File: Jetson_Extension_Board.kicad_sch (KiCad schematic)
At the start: 2 parts, among them J6 40_Pin_Jetson_Connector, SW1 SW_Push_DPDT

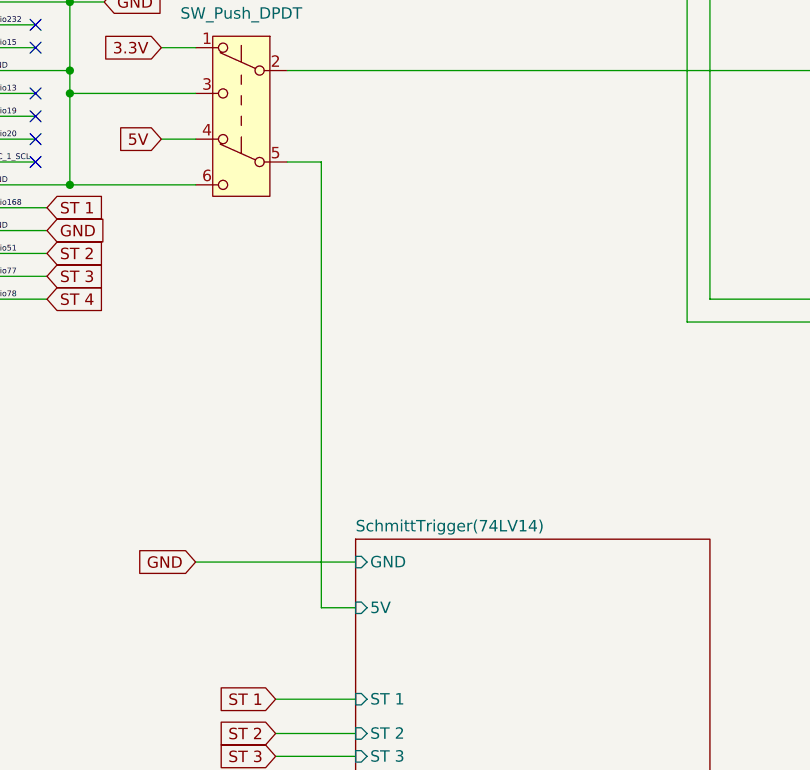
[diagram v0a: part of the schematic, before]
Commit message: Pluh 1 and 2 removed, main file is updated version
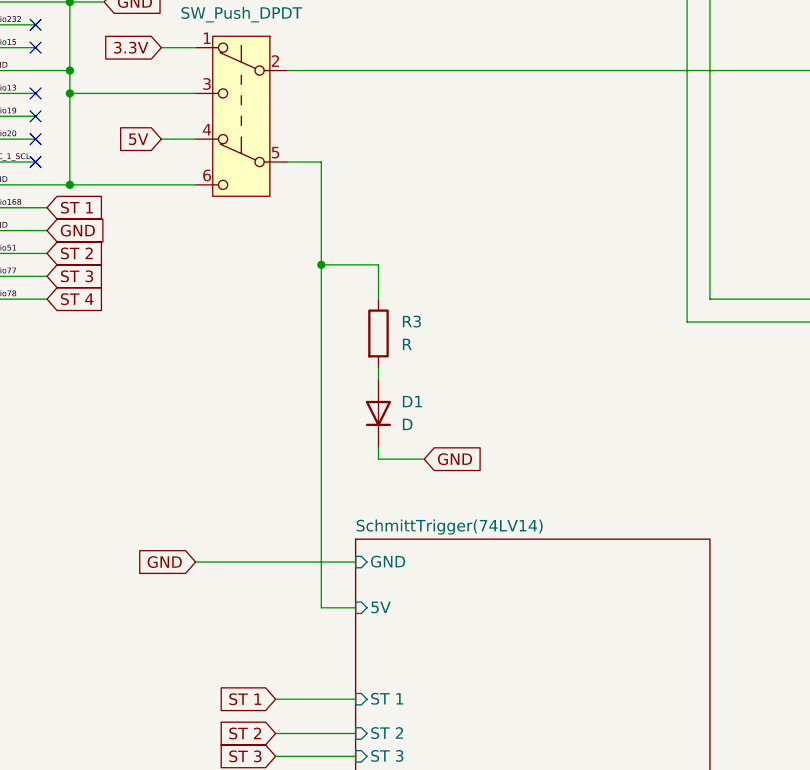
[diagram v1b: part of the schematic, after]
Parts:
- added D1: D, symbol Device:D
- added R3: R, symbol Device:R
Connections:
- net GND: now also D1.1 (K)
- net SchmittTrigger(74LV14)/5V: now also R3.1
- new net: D1.2 (A), R3.2
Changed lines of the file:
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@@
+		(color 0 0 0 0)
+	)
+	(junction
+		(at 121.92 118.11)
+		(diameter 0)
 		(color 0 0 0 0)
 	)
@@
 	(wire
 		(pts
+			(xy 128.27 138.43) (xy 128.27 139.7)
+		)
+		(stroke
+			(width 0)
+			(type default)
+		)
+	)
+	(wire
+		(pts
 			(xy 118.11 106.68) (xy 121.92 106.68)
 		)
@@
 	(wire
 		(pts
+			(xy 128.27 118.11) (xy 121.92 118.11)
+		)
+		(stroke
+			(width 0)
+			(type default)
+		)
+	)
+	(wire
+		(pts
 			(xy 104.14 93.98) (xy 107.95 93.98)
 		)
@@
 	(wire
 		(pts
+			(xy 128.27 130.81) (xy 128.27 129.54)
+		)
+		(stroke
+			(width 0)
+			(type default)
+		)
+	)
+	(wire
+		(pts
 			(xy 177.8 96.52) (xy 118.11 96.52)
 		)
@@
 	(wire
 		(pts
-			(xy 121.92 156.21) (xy 121.92 106.68)
+			(xy 121.92 156.21) (xy 121.92 118.11)
+		)
+		(stroke
+			(width 0)
+			(type default)
+		)
+	)
+	(wire
+		(pts
+			(xy 121.92 118.11) (xy 121.92 106.68)
 		)
 		(stroke
@@
 	(wire
 		(pts
+			(xy 128.27 139.7) (xy 133.35 139.7)
+		)
+		(stroke
+			(width 0)
+			(type default)
+		)
+	)
+	(wire
+		(pts
 			(xy 63.5 73.66) (xy 72.39 73.66)
 		)
@@
 		(pts
 			(xy 177.8 66.04) (xy 195.58 66.04)
+		)
+		(stroke
+			(width 0)
+			(type default)
+		)
+	)
+	(wire
+		(pts
+			(xy 128.27 121.92) (xy 128.27 118.11)
 		)
 		(stroke
@@
 				)
 				(justify right)
+				(hide yes)
+			)
+		)
+	)
+	(global_label "GND"
+		(shape input)
+		(at 133.35 139.7 0)
+		(fields_autoplaced yes)
+		(effects
+			(font
+				(size 1.27 1.27)
+			)
+			(justify left)
+		)
+		(property "Intersheetrefs" "${INTERSHEET_REFS}"
+			(at 140.2057 139.7 0)
+			(effects
+				(font
+					(size 1.27 1.27)
+				)
+				(justify left)
 				(hide yes)
 			)
@@
 	)
 	(symbol
+		(lib_id "Device:R")
+		(at 128.27 125.73 0)
+		(unit 1)
+		(exclude_from_sim no)
+		(in_bom yes)
+		(on_board yes)
+		(dnp no)
+		(fields_autoplaced yes)
+		(property "Reference" "R3"
+			(at 130.81 124.4599 0)
+			(effects
+				(font
+					(size 1.27 1.27)
+				)
+				(justify left)
+			)
+		)
+		(property "Value" "R"
+			(at 130.81 126.9999 0)
+			(effects
+				(font
+					(size 1.27 1.27)
+				)
+				(justify left)
+			)
+		)
+		(property "Footprint" ""
+			(at 126.492 125.73 90)
+			(effects
+				(font
+					(size 1.27 1.27)
+				)
+				(hide yes)
+			)
+		)
+		(property "Datasheet" "~"
+			(at 128.27 125.73 0)
+			(effects
+				(font
+					(size 1.27 1.27)
+				)
+				(hide yes)
+			)
+		)
+		(property "Description" "Resistor"
+			(at 128.27 125.73 0)
+			(effects
+				(font
+					(size 1.27 1.27)
+				)
+				(hide yes)
+			)
+		)
+		(pin "1"
+		)
+		(pin "2"
+		)
+		(instances
+			(project ""
+				(path "/fac81d63-8655-47f4-bf8e-62708c29b8c6"
+					(reference "R3")
+					(unit 1)
+				)
+			)
+		)
+	)
+	(symbol
 		(lib_id "Connector_Generic:Conn_02x20_Odd_Even")
 		(at 77.47 96.52 0)
@@
 					(unit 1)
 				)
+			)
+		)
+	)
+	(symbol
+		(lib_id "Device:D")
+		(at 128.27 134.62 90)
+		(unit 1)
+		(exclude_from_sim no)
+		(in_bom yes)
+		(on_board yes)
+		(dnp no)
+		(fields_autoplaced yes)
+		(property "Reference" "D1"
+			(at 130.81 133.3499 90)
+			(effects
+				(font
+					(size 1.27 1.27)
+				)
+				(justify right)
+			)
+		)
+		(property "Value" "D"
+			(at 130.81 135.8899 90)
+			(effects
+				(font
+					(size 1.27 1.27)
+				)
+				(justify right)
+			)
+		)
+		(property "Footprint" ""
+			(at 128.27 134.62 0)
+			(effects
+				(font
+					(size 1.27 1.27)
+				)
+				(hide yes)
+			)
+		)
+		(property "Datasheet" "~"
+			(at 128.27 134.62 0)
+			(effects
+				(font
+					(size 1.27 1.27)
+				)
+				(hide yes)
+			)
+		)
+		(property "Description" "Diode"
+			(at 128.27 134.62 0)
+			(effects
+				(font
+					(size 1.27 1.27)
+				)
+				(hide yes)
+			)
+		)
+		(property "Sim.Device" "D"
+			(at 128.27 134.62 0)
+			(effects
+				(font
+					(size 1.27 1.27)
+				)
+				(hide yes)
+			)
+		)
+		(property "Sim.Pins" "1=K 2=A"
+			(at 128.27 134.62 0)
+			(effects
+				(font
+					(size 1.27 1.27)
+				)
+				(hide yes)
+			)
+		)
+		(pin "1"
+		)
+		(pin "2"
+		)
+		(instances
+			(project ""
+				(path "/fac81d63-8655-47f4-bf8e-62708c29b8c6"
+					(reference "D1")
+					(unit 1)
+				)

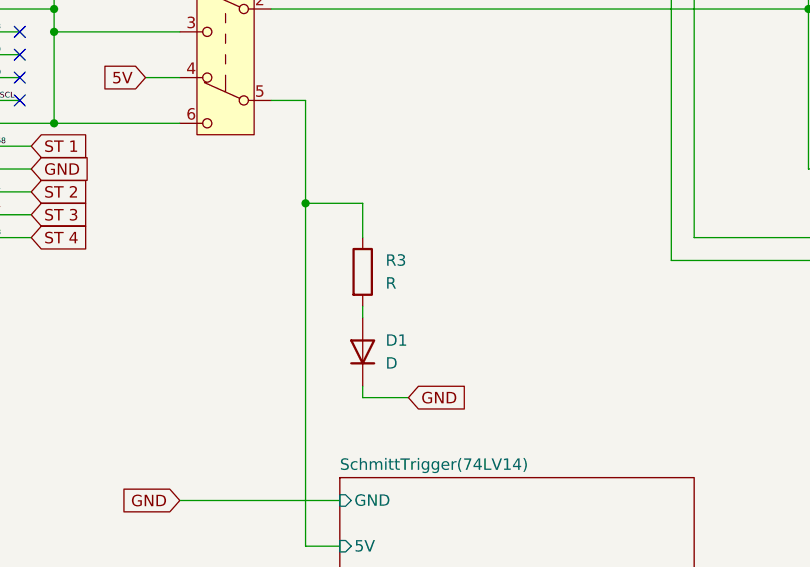
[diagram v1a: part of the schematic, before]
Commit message: LEDS
consolidated file, added diode and resistor (look over), and silkscreen errors present
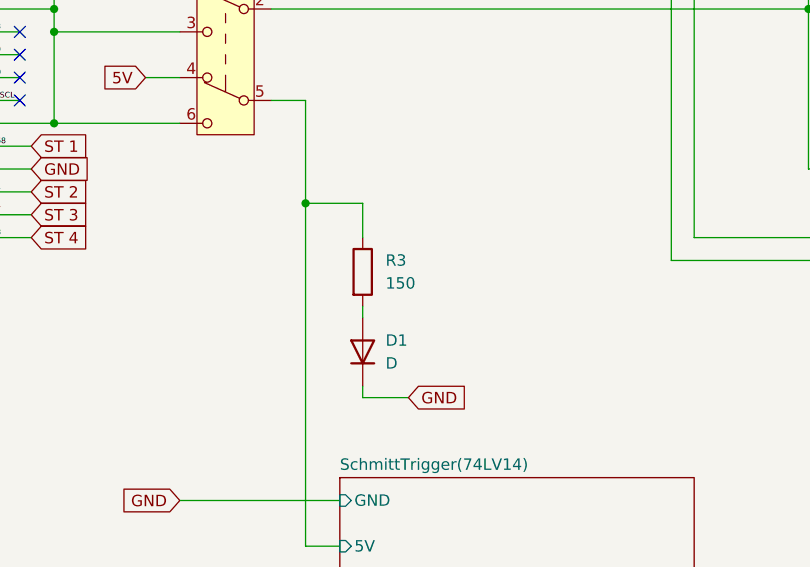
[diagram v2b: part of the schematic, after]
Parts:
- D1: footprint (none) -> LED_SMD:LED_LiteOn_LTST-C295K_1.6x0.8mm
- R3: value R -> 150; footprint (none) -> Resistor_SMD:R_1206_3216Metric
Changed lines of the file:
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@@
 			)
 		)
-		(property "Value" "R"
+		(property "Value" "150"
 			(at 130.81 126.9999 0)
 			(effects
@@
 			)
 		)
-		(property "Footprint" ""
+		(property "Footprint" "Resistor_SMD:R_1206_3216Metric"
 			(at 126.492 125.73 90)
 			(effects
@@
 			)
 		)
-		(property "Footprint" ""
+		(property "Footprint" "LED_SMD:LED_LiteOn_LTST-C295K_1.6x0.8mm"
 			(at 128.27 134.62 0)
 			(effects

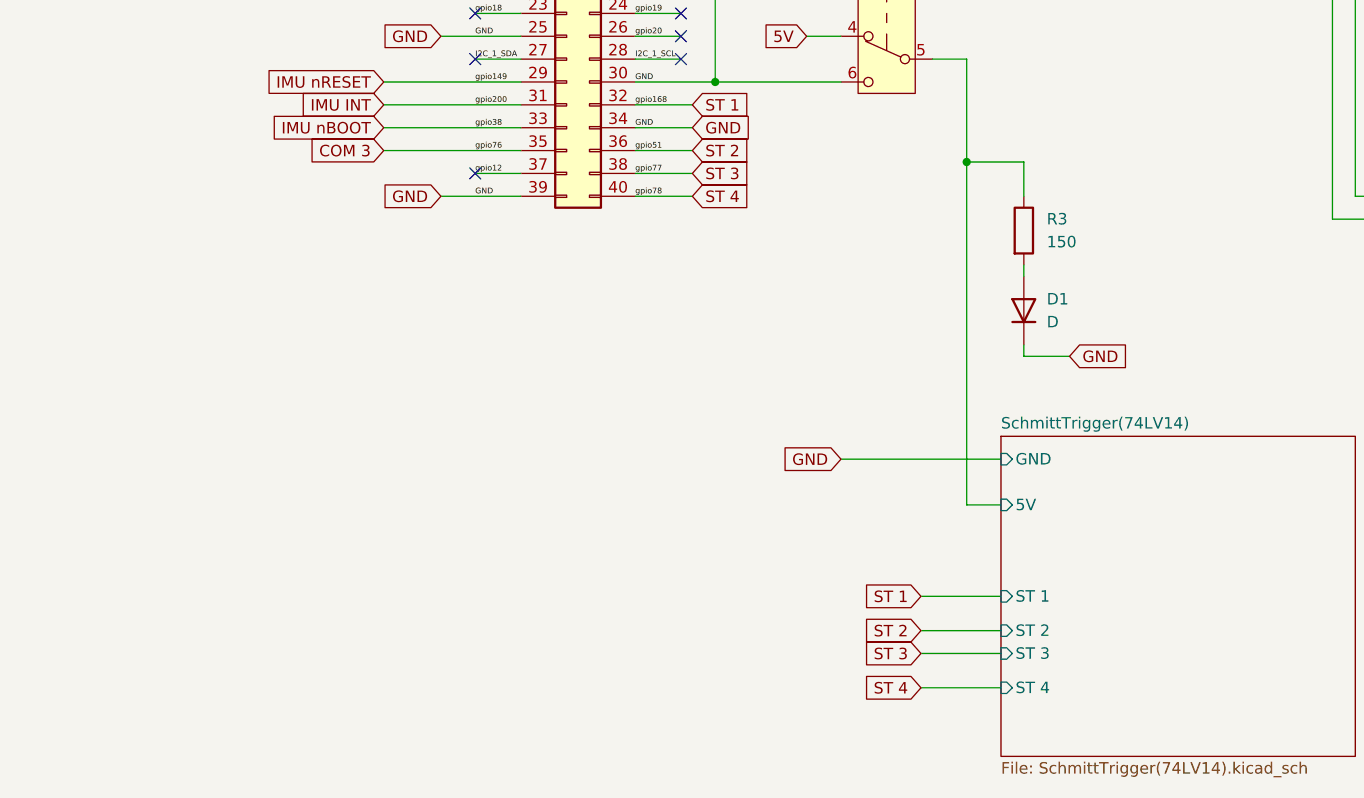
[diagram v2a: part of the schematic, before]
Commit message: Added Correct LED
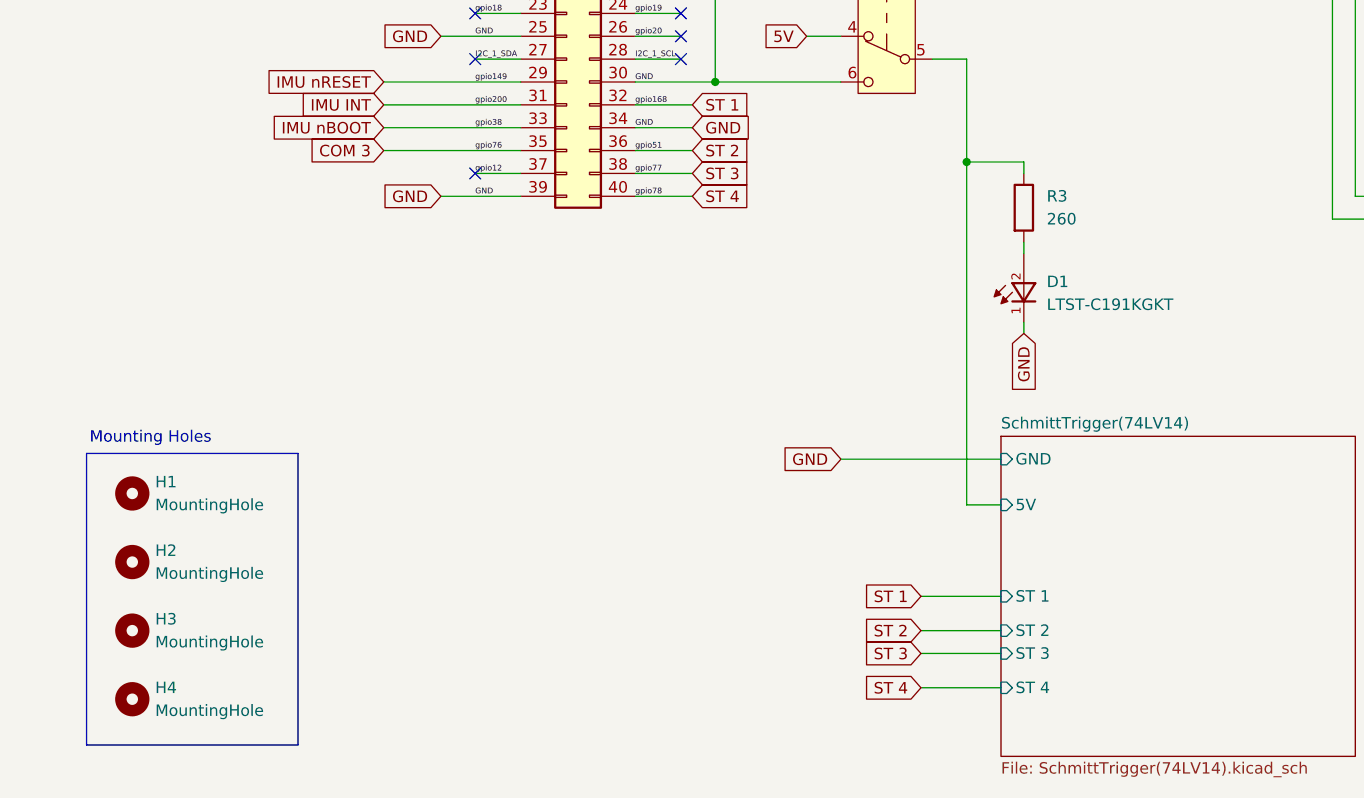
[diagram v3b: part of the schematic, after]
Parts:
- removed D1: D, LED_SMD:LED_LiteOn_LTST-C295K_1.6x0.8mm, symbol Device:D
- added D1: LTST-C191KGKT, LTST_C191KGKT:0603, symbol LTST-C191KGKT:LTST-C191KGKT
- added H1, H2, H3, H4: MountingHole, MountingHole:MountingHole_2.1mm, symbol Mechanical:MountingHole
- R3: value 150 -> 260
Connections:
- net GND: now also D1.1
- net at R3.2: now also D1.2
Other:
- note added: "Mounting Holes"
- moved on the sheet: R3
